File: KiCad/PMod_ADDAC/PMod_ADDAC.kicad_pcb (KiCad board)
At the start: 2 copper layers, 35.6 x 21.1 mm, 22 parts, among them J1 Conn_01x12_Male, J2 AudioJack2_SwitchT, U1 TSX632

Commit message: R2R updated
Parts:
- removed C1: 1u, Capacitor_SMD:C_0805_2012Metric_Pad1.15x1.40mm_HandSolder
- added C2: 100, Capacitor_SMD:C_0805_2012Metric_Pad1.15x1.40mm_HandSolder, F.Cu at (53.3, 46.0)
- added R18: 1k, Resistor_SMD:R_0805_2012Metric_Pad1.15x1.40mm_HandSolder, F.Cu at (67.1, 48.3)
- added R19: 1k, Resistor_SMD:R_0805_2012Metric_Pad1.15x1.40mm_HandSolder, F.Cu at (63.0, 48.3)
- added REF**: OSHW-Logo_5.7x6mm_SilkScreen, Symbol:OSHW-Logo_5.7x6mm_SilkScreen, B.Cu at (65.5, 50.3)
- R17: value 8k -> 2k
- moved JP1 12.8 mm to (61.5, 51.2), turned to 270 degrees
- moved U1 10.3 mm to (54.8, 49.9), turned to 180 degrees
- moved R17 7.70 mm to (59.7, 46.0), turned to 0 degrees
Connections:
- JP1 pad 2: Net-(J2-PadT) -> Net-(JP1-Pad2)
- R17 pad 1: Net-(JP1-Pad1) -> GND
- R17 pad 2: Net-(C1-Pad1) -> Net-(JP1-Pad1)
- U1 pad 1: Net-(J2-PadT) -> Net-(JP1-Pad2)
- U1 pad 2: Net-(JP1-Pad1) -> Net-(JP1-Pad2)
- U1 pad 3: Net-(J2-PadT) -> Net-(JP1-Pad1)
- U1 pad 5: (no net) -> GND
- U1 pad 6: (no net) -> Net-(U1-Pad6)
- U1 pad 7: (no net) -> Net-(U1-Pad6)
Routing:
- net Net-(JP1-Pad1): track 0.00 -> 14.4 mm
- net VCC: track 2.54 -> 15.0 mm
- net Net-(JP1-Pad2): track 0.00 -> 11.9 mm
- net GND: track 1.57 -> 11.5 mm, vias 1 -> 2
- net Net-(C1-Pad1): track 2.01 -> 0.00 mm
- net Net-(U1-Pad6): track 0.00 -> 1.27 mm
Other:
- board text added: "GND"
- board text added: "R = 1k"
- board text added: "R = 2k"
- board text added: "T"

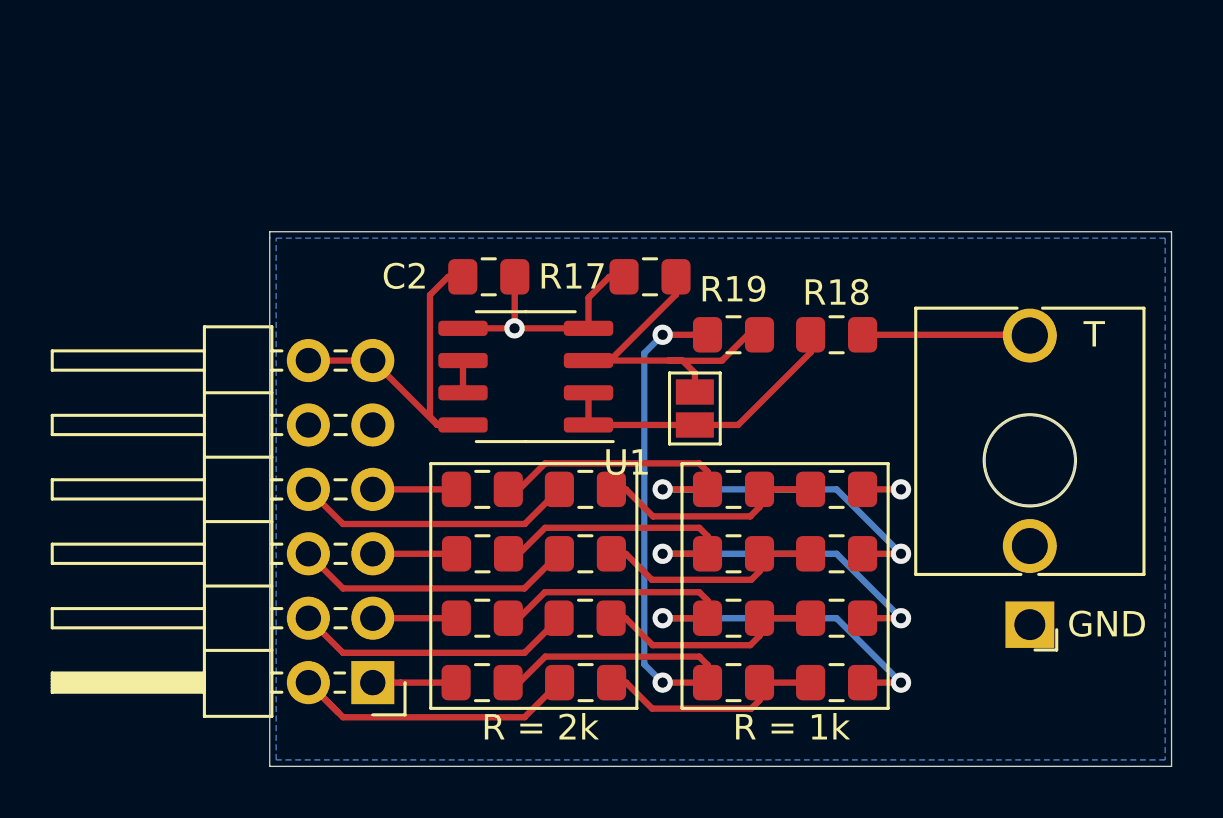
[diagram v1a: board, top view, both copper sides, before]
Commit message: fixed R2R orientation
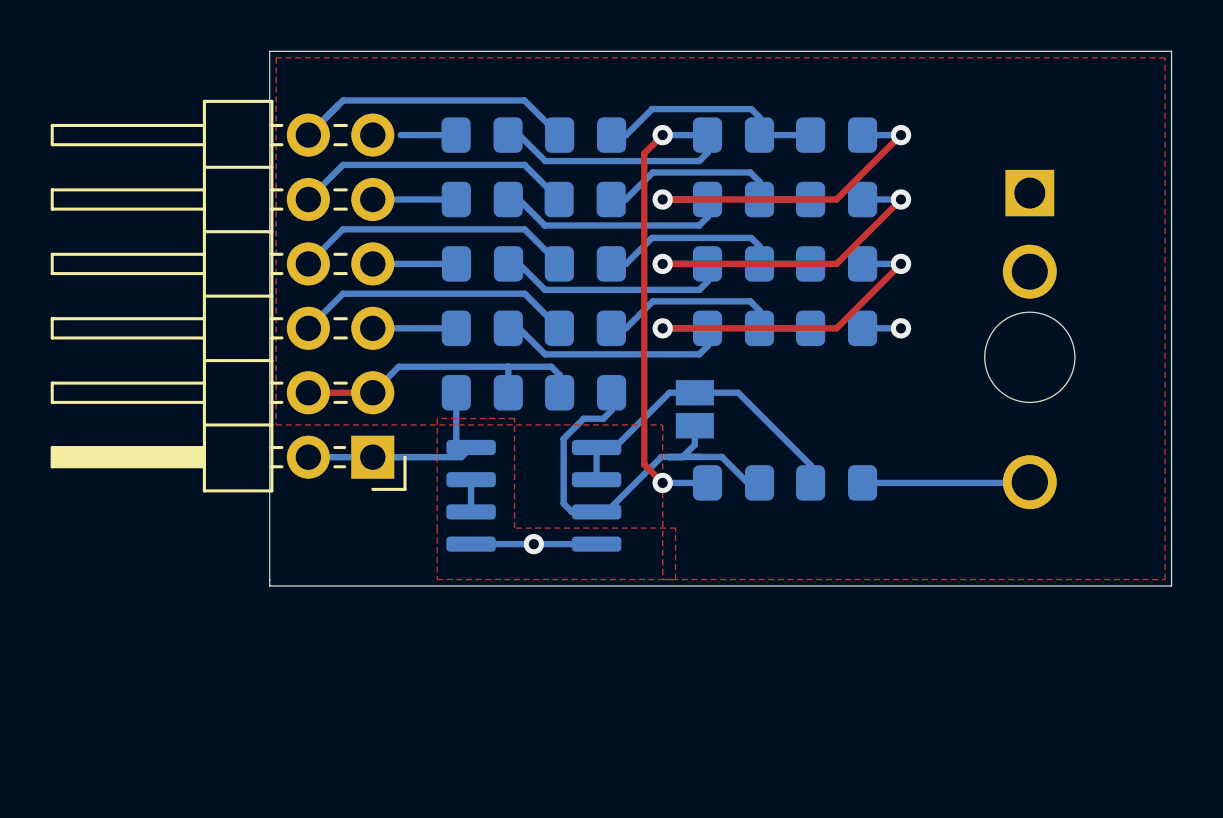
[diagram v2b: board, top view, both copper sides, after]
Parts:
- removed REF**: OSHW-Logo_5.7x6mm_SilkScreen, Symbol:OSHW-Logo_5.7x6mm_SilkScreen
- C2, J2, JP1, R1, R10, R11, R12, R13, R14, R15, R16, R17, R18, R19, R2, R3, R4, R5, R6, R7, R8, R9, U1: moved to B.Cu
- moved R1 21.6 mm to (53.1, 40.4)
- moved R10 21.6 mm to (67.1, 40.4)
- moved R2 21.6 mm to (57.2, 40.4)
- moved R9 21.6 mm to (63.0, 40.4)
- moved J2 17.0 mm to (74.7, 42.7)
- moved R11 16.5 mm to (63.0, 42.9)
- moved R12 16.5 mm to (67.1, 42.9)
- moved R3 16.5 mm to (53.1, 42.9)
- moved R4 16.5 mm to (57.1, 42.9)
- moved R13 11.4 mm to (63.0, 45.5)
- moved R14 11.4 mm to (67.1, 45.5)
- moved R5 11.4 mm to (53.1, 45.5)
- moved R6 11.4 mm to (57.1, 45.5)
- moved J1 8.89 mm to (48.8, 53.1)
- moved R15 6.35 mm to (63.0, 48.0)
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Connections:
- J1 pad 1: Net-(J1-Pad1) -> VCC
- J1 pad 10: GND -> Net-(J1-Pad10)
- J1 pad 11: VCC -> Net-(J1-Pad11)
- J1 pad 12: VCC -> Net-(J1-Pad12)
- J1 pad 2: Net-(J1-Pad2) -> VCC
- J1 pad 3: Net-(J1-Pad3) -> GND
- J1 pad 4: Net-(J1-Pad4) -> GND
- J1 pad 9: GND -> Net-(J1-Pad9)
- R1 pad 1: Net-(J1-Pad1) -> Net-(J1-Pad11)
- R2 pad 1: Net-(J1-Pad2) -> Net-(J1-Pad12)
- R3 pad 1: Net-(J1-Pad3) -> Net-(J1-Pad9)
- R4 pad 1: Net-(J1-Pad4) -> Net-(J1-Pad10)
- R5 pad 1: Net-(J1-Pad5) -> Net-(J1-Pad7)
- R6 pad 1: Net-(J1-Pad6) -> Net-(J1-Pad8)
- R7 pad 1: Net-(J1-Pad7) -> Net-(J1-Pad5)
- R8 pad 1: Net-(J1-Pad8) -> Net-(J1-Pad6)
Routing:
- net Net-(J1-Pad12): track 0.00 -> 12.7 mm
- net Net-(J1-Pad2): track 12.7 -> 0.00 mm
- net Net-(J1-Pad10): track 0.00 -> 11.0 mm
- net Net-(J1-Pad4): track 11.0 -> 0.00 mm
- net GND: track 11.5 -> 18.7 mm
- net VCC: track 15.0 -> 9.23 mm
- net Net-(JP1-Pad1): track 14.4 -> 18.0 mm
- net Net-(J1-Pad9): track 0.00 -> 3.29 mm
- net Net-(J1-Pad3): track 3.29 -> 0.00 mm
- net Net-(J1-Pad1): track 3.28 -> 0.00 mm
- net Net-(J1-Pad11): track 0.00 -> 2.18 mm
- net Net-(JP1-Pad2): track 11.9 -> 12.5 mm
- added copper zone on F.Cu, net GND
- removed copper zone on B.Cu, net GND
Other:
- outline, holes or cut-outs redrawn

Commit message: kicad update
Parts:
- removed C2: 100, Capacitor_SMD:C_0805_2012Metric_Pad1.15x1.40mm_HandSolder
- removed U1: TSX632, Package_SO:SOIC-8_3.9x4.9mm_P1.27mm
- added C1: 100, Capacitor_SMD:C_0805_2012Metric_Pad1.15x1.40mm_HandSolder, F.Cu at (75.8, 23.6)
- added C12: variable, Capacitor_THT:C_Disc_D5.0mm_W2.5mm_P5.00mm, F.Cu at (28.7, 51.1)
- added C8: 100n, Capacitor_SMD:C_0805_2012Metric_Pad1.15x1.40mm_HandSolder, F.Cu at (7.45, 52.8)
- added C9: variable, Capacitor_THT:C_Disc_D5.0mm_W2.5mm_P5.00mm, F.Cu at (28.7, 47.1)
- added J3: Conn_01x16_Male, Connector_PinHeader_2.54mm:PinHeader_2x08_P2.54mm_Vertical, F.Cu at (7.40, 12.7)
- added J4: AudioJack2_SwitchT, Audio_conn:Jack_3.5mm_QingPu_WQP-PJ398SM_Vertical_CircularHoles, F.Cu at (21.6, 37.8)
- added J5: AudioJack2_SwitchT, Audio_conn:Jack_3.5mm_QingPu_WQP-PJ398SM_Vertical_CircularHoles, F.Cu at (10.6, 37.8)
- added R20: 100k, Resistor_SMD:R_0805_2012Metric_Pad1.15x1.40mm_HandSolder, F.Cu at (12.2, 52.8)
- added RV2: 10k, Potentiometer_THT:Potentiometer_Bourns_3339P_Vertical, F.Cu at (31.8, 43.0)
- J2: value AudioJack2_SwitchT -> Basys power; footprint Audio_conn:Jack_3.5mm_QingPu_WQP-PJ398SM_Vertical_CircularHoles -> Connector_PinHeader_2.54mm:PinHeader_1x02_P2.54mm_Vertical; moved to F.Cu
- JP1, R1, R10, R11, R12, R13, R14, R15, R19, R2, R3, R4, R5, R6, R7, R8: moved to F.Cu
- R16, R17: value 2k -> 1k; moved to F.Cu
- R18, R9: value 1k -> 2k; moved to F.Cu
- moved J2 67.2 mm to (14.6, 12.7), turned to 0 degrees
- moved R5 40.6 mm to (75.8, 11.8)
- moved J1 40.4 mm to (50.3, 12.7), turned to 0 degrees
- moved R18 38.8 mm to (80.6, 17.7)
- moved R8 38.1 mm to (75.8, 14.8)
- moved R15 37.6 mm to (80.6, 14.8)
- moved R11 35.7 mm to (80.6, 11.8)
- moved JP1 35.6 mm to (80.4, 21.0), turned to 0 degrees
- moved R17 35.2 mm to (75.8, 20.7)
- moved R7 35.2 mm to (71.1, 17.7)
- moved R2 31.8 mm to (71.1, 11.8)
- moved R4 31.4 mm to (71.1, 14.8)
- moved R13 30.6 mm to (75.8, 17.7)
- moved R1 28.8 mm to (66.3, 14.8)
- moved R19 28.7 mm to (71.1, 26.6), turned to 0 degrees
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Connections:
- R10 pad 1: Net-(R10-Pad1) -> Net-(JP1-Pad1)
- R10 pad 2: Net-(R10-Pad2) -> Net-(R1-Pad2)
- R11 pad 1: Net-(R10-Pad2) -> Net-(R1-Pad2)
- R16 pad 2: GND -> Net-(R16-Pad2)
- R17 pad 1: GND -> Net-(R16-Pad2)
- R17 pad 2: Net-(JP1-Pad1) -> Net-(R17-Pad2)
- R18 pad 1: Net-(JP1-Pad2) -> Net-(R17-Pad2)
- R18 pad 2: Net-(J2-PadT) -> GND
- R19 pad 1: Net-(JP1-Pad1) -> Net-(JP1-Pad2)
- R19 pad 2: Net-(R1-Pad2) -> DAC_D_out
- R2 pad 2: Net-(R10-Pad1) -> Net-(R11-Pad2)
- R3 pad 2: Net-(R10-Pad2) -> Net-(R12-Pad2)
- R4 pad 2: Net-(R11-Pad2) -> Net-(R13-Pad2)
- R5 pad 2: Net-(R12-Pad2) -> Net-(R14-Pad2)
- R6 pad 2: Net-(R13-Pad2) -> Net-(R15-Pad2)
- R7 pad 2: Net-(R14-Pad2) -> Net-(R16-Pad2)
- R8 pad 2: Net-(R15-Pad2) -> Net-(R17-Pad2)
- R9 pad 1: Net-(R1-Pad2) -> GND
- R9 pad 2: Net-(R10-Pad1) -> Net-(JP1-Pad1)
